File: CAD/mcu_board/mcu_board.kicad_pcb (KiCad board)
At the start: 2 copper layers, 151 parts, among them J1 2.1MM BARREL, J2 E5908-5VC145-L, J3 E5908-5VC145-L, J4 E5908-5VC145-L, SW1 SW_EN, U1 Teensy3.6, U2 AUDIOSHIELD, U3 LM1117-ADJ, U4 TLC5947DAP

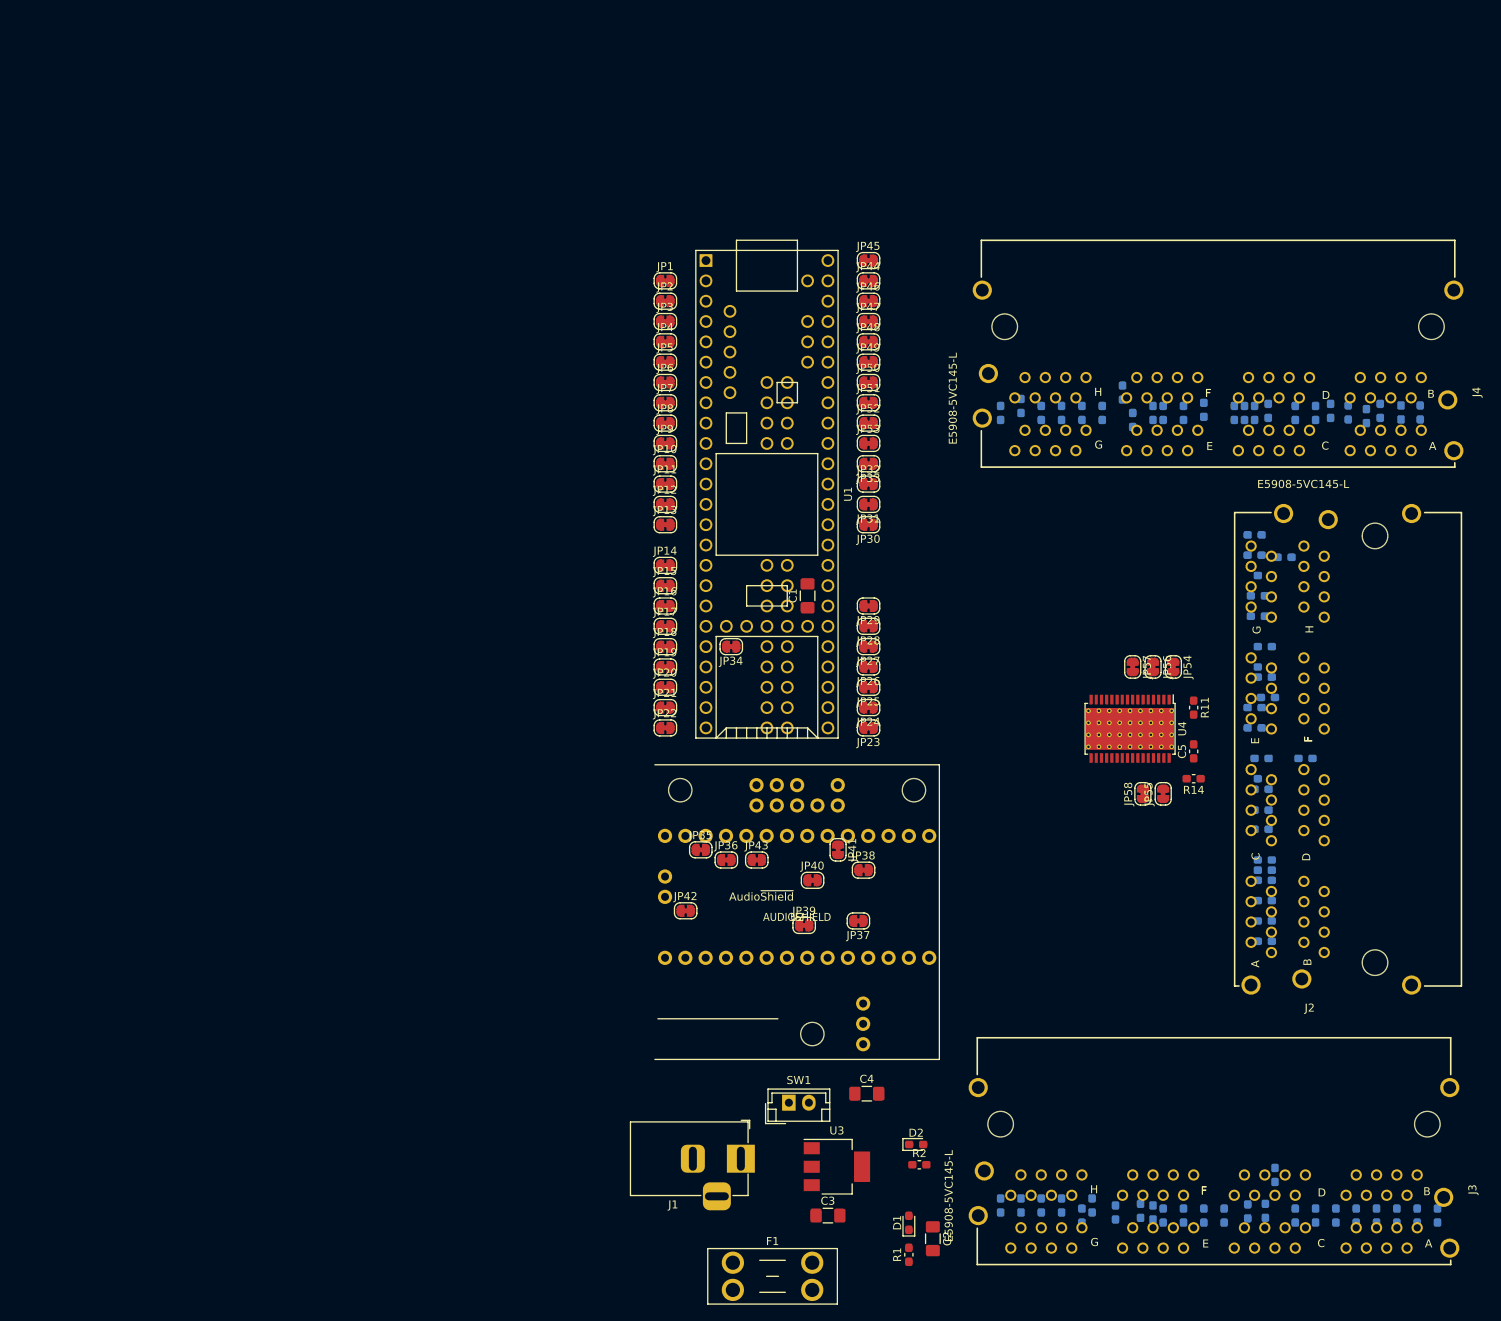
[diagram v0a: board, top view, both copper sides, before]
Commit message: finishes most routing
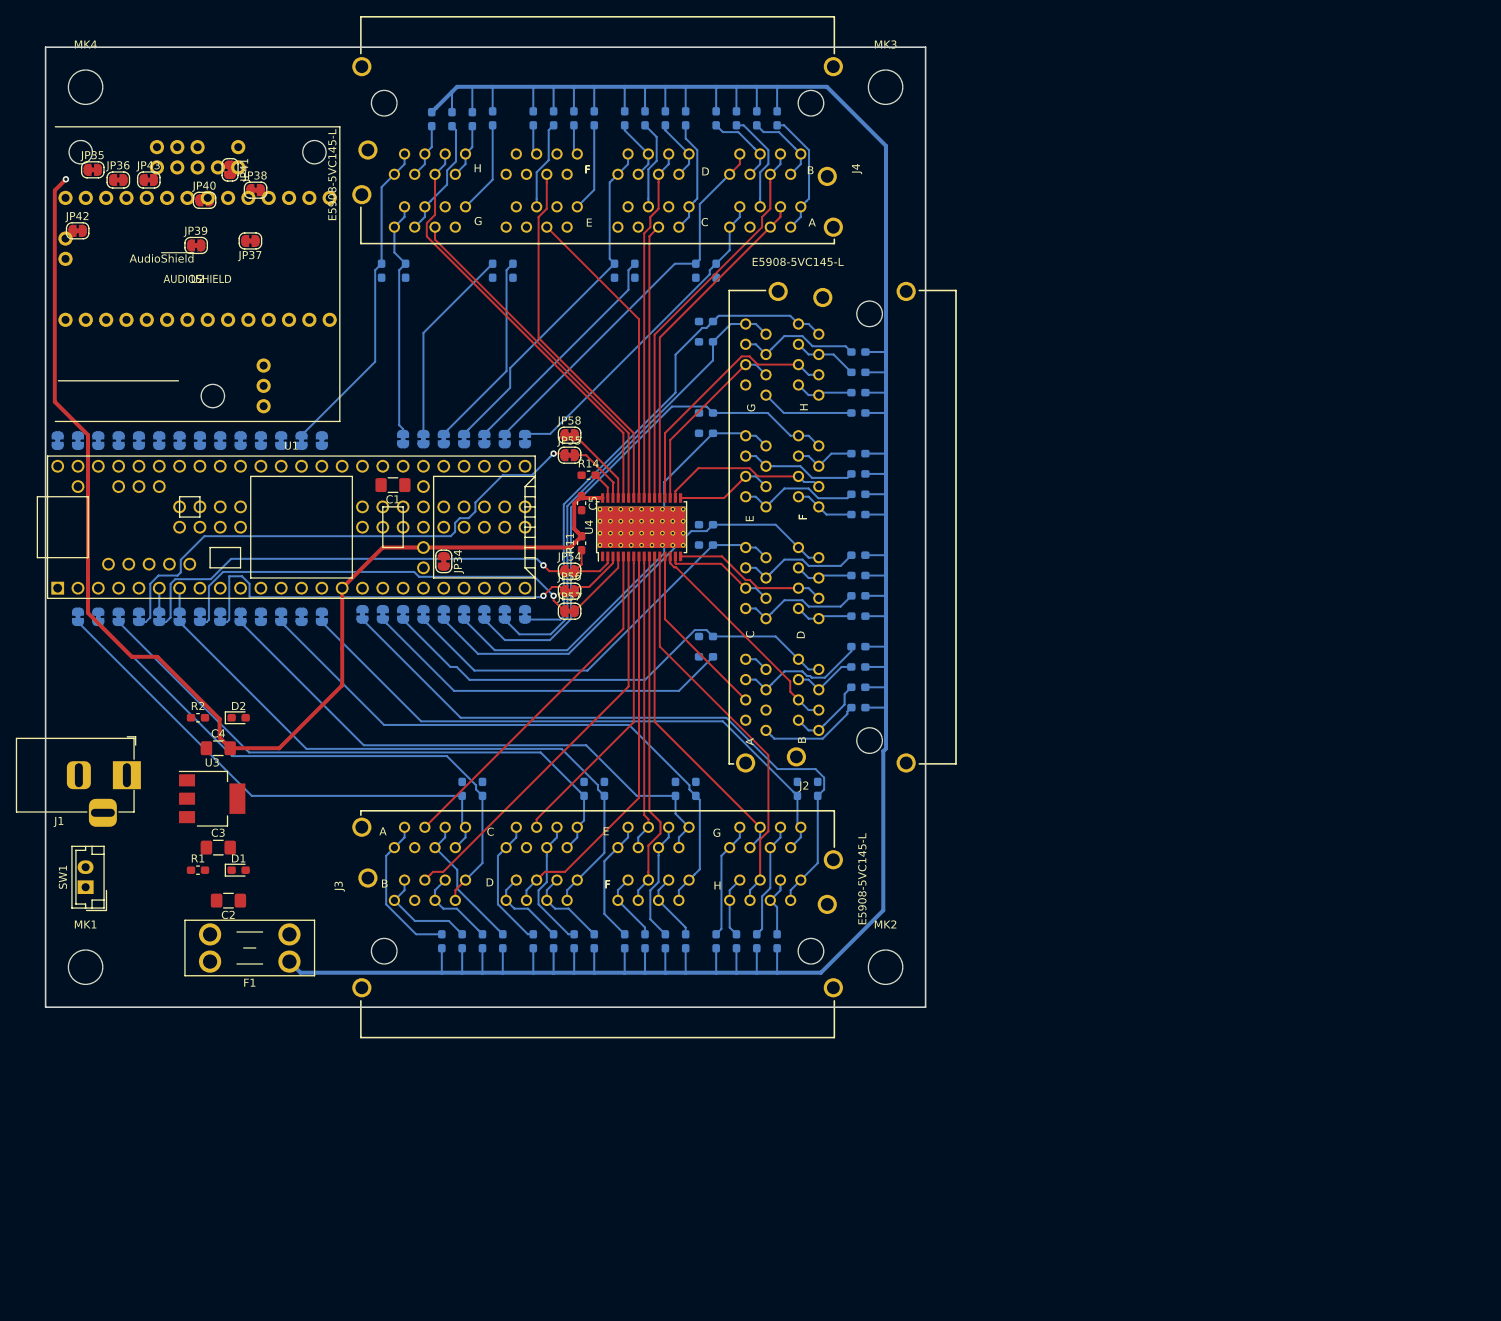
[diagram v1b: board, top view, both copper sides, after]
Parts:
- added MK1: Mounting_Hole, MountingHole:MountingHole_4.3mm_M4, F.Cu at (5.00, 115.0)
- added MK2: Mounting_Hole, MountingHole:MountingHole_4.3mm_M4, F.Cu at (105.0, 115.0)
- added MK3: Mounting_Hole, MountingHole:MountingHole_4.3mm_M4, F.Cu at (105.0, 5.00)
- added MK4: Mounting_Hole, MountingHole:MountingHole_4.3mm_M4, F.Cu at (5.00, 5.00)
- JP1, JP10, JP11, JP12, JP13, JP14, JP15, JP16, JP17, JP18, JP19, JP2, JP20, JP21, JP22, JP23, JP24, JP25, JP26, JP27, JP28, JP29, JP3, JP30, JP31, JP32, JP33, JP4, JP44, JP45, JP46, JP47, JP48, JP49, JP5, JP50, JP51, JP52, JP53, JP6, JP7, JP8, JP9: moved to B.Cu
- moved R76 126.7 mm to (52.1, 111.8), turned to 270 degrees
- moved R64 126.7 mm to (49.5, 111.8), turned to 270 degrees
- moved R62 123.8 mm to (52.1, 92.7)
- moved R74 119.3 mm to (54.6, 92.7)
- moved R75 116.9 mm to (54.6, 111.8), turned to 90 degrees
- moved R63 116.9 mm to (57.1, 111.8), turned to 90 degrees
- moved JP35 114.0 mm to (5.90, 15.3)
- moved JP36 114.0 mm to (9.09, 16.6)
- moved JP37 114.0 mm to (25.6, 24.2)
- moved JP38 114.0 mm to (26.2, 17.9)
- moved JP39 114.0 mm to (18.8, 24.8)
- moved JP40 114.0 mm to (19.9, 19.1)
- moved JP41 114.0 mm to (23.1, 15.3)
- moved JP42 114.0 mm to (4.01, 22.9)
- moved JP43 114.0 mm to (12.9, 16.6)
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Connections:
- JP1 pad 1: /SW_0 -> /SW_16
- JP11 pad 1: /SW_5 -> /SW_21
- JP13 pad 1: /SW_6 -> /SW_22
- JP14 pad 1: /SW_7 -> /SW_23
- JP2 pad 1: /SW_1 -> /SW_17
- JP23 pad 1: /SW_17 -> /SW_0
- JP24 pad 1: /SW_18 -> /SW_1
- JP25 pad 1: /SW_19 -> /SW_2
- JP26 pad 1: /SW_20 -> /SW_3
- JP27 pad 1: /SW_21 -> /SW_4
- JP28 pad 1: /SW_21 -> /SW_5
- JP29 pad 1: /SW_22 -> /SW_6
- JP3 pad 1: /SW_2 -> /SW_18
- JP31 pad 1: /SW_23 -> /SW_7
- JP6 pad 1: /SW_3 -> /SW_19
- JP9 pad 1: /SW_4 -> /SW_20
- U4 pad 10: /LED_5 -> /LED_21
- U4 pad 11: /LED_6 -> /LED_22
- U4 pad 12: /LED_7 -> /LED_23
- U4 pad 21: /LED_16 -> /LED_0
- U4 pad 22: /LED_17 -> /LED_1
- U4 pad 23: /LED_18 -> /LED_2
- U4 pad 24: /LED_19 -> /LED_3
- U4 pad 25: /LED_20 -> /LED_4
- U4 pad 26: /LED_21 -> /LED_5
- U4 pad 27: /LED_22 -> /LED_6
- U4 pad 28: /LED_23 -> /LED_7
- U4 pad 5: /LED_0 -> /LED_16
- U4 pad 6: /LED_1 -> /LED_17
- U4 pad 7: /LED_2 -> /LED_18
- U4 pad 8: /LED_3 -> /LED_19
- U4 pad 9: /LED_4 -> /LED_20
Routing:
- net +12V: track 0.00 -> 370.5 mm
- net +3V3: track 0.00 -> 153.1 mm, vias 0 -> 1
- net /SW_23: track 0.00 -> 83.0 mm
- net /SW_19: track 0.00 -> 77.4 mm
- net /SW_22: track 0.00 -> 75.6 mm
- net /SW_21: track 0.00 -> 75.5 mm
- net /SW_18: track 0.00 -> 74.5 mm
- net /SW_17: track 0.00 -> 71.8 mm
- net /SW_20: track 0.00 -> 71.1 mm
- net /XLAT: track 0.00 -> 66.7 mm, vias 0 -> 1
- net /SW_13: track 0.00 -> 65.2 mm
- net /SW_15: track 0.00 -> 64.4 mm
- net /SW_16: track 0.00 -> 64.2 mm
- net /SW_9: track 0.00 -> 59.7 mm
- net /SW_14: track 0.00 -> 59.5 mm
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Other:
- board outline added: 110 x 120 mm

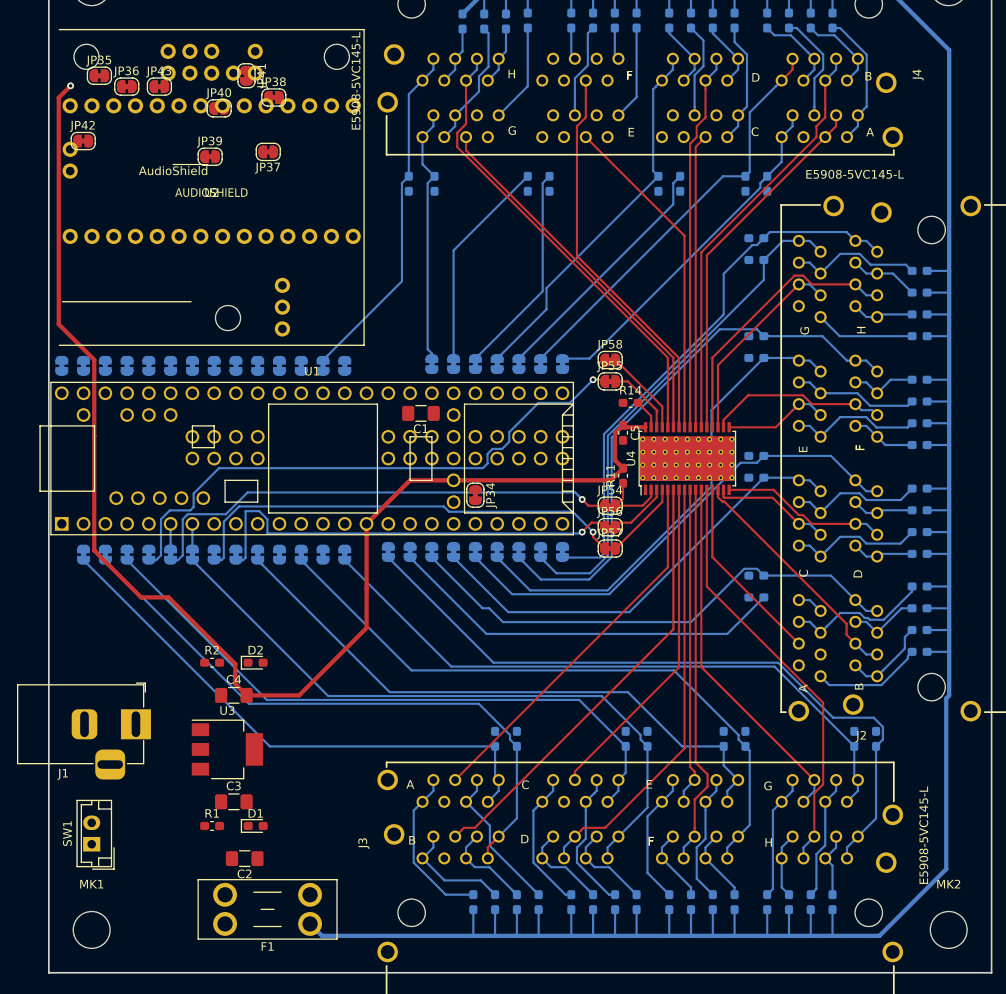
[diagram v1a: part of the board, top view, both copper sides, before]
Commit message: finish all routing but GND
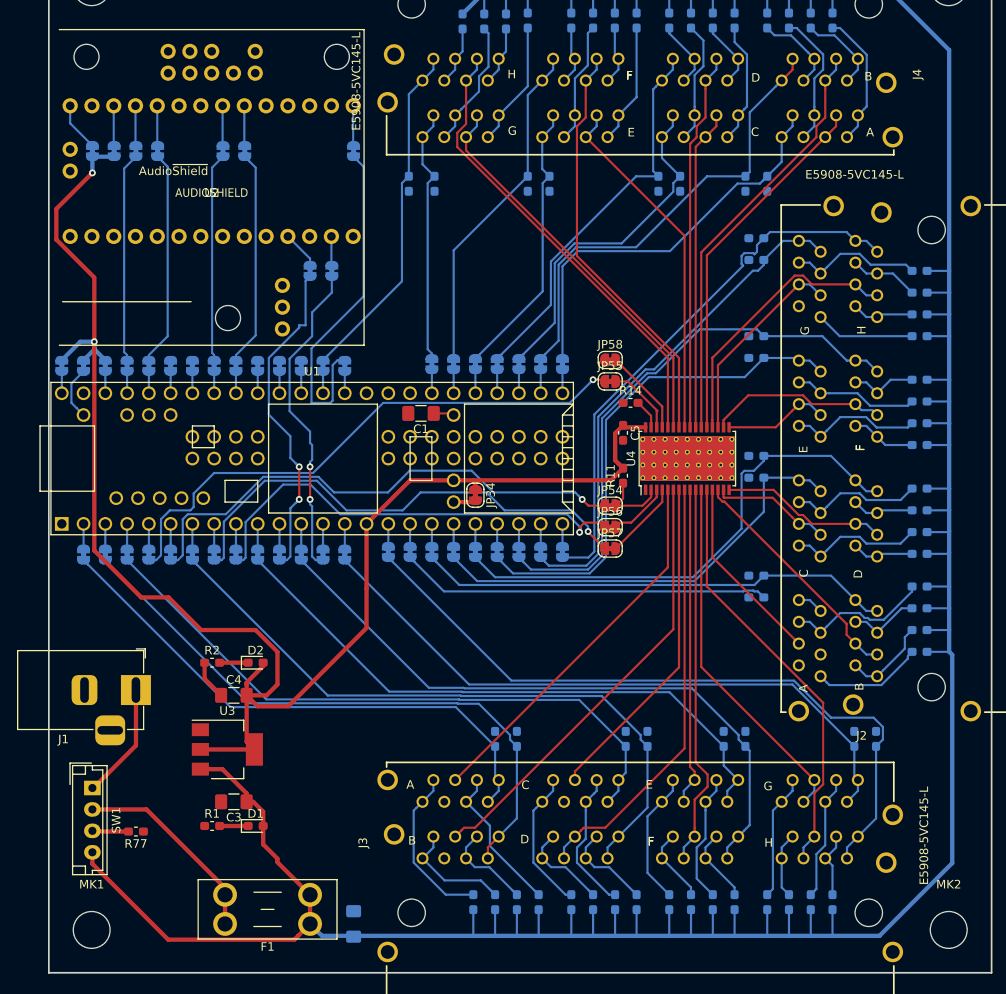
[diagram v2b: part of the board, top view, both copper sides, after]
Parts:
- added R77: 1K, Resistor_SMD:R_0603_1608Metric_Pad1.05x0.95mm_HandSolder, F.Cu at (10.2, 103.5)
- C2, JP35, JP36, JP37, JP38, JP39, JP40, JP41, JP42, JP43: moved to B.Cu
- R70: value R_L -> 1K
- SW1: value SW_EN -> SW_SPST_LED; footprint Connector_JST:JST_EH_B02B-EH-A_1x02_P2.50mm_Vertical -> Connector_JST:JST_EH_B04B-EH-A_1x04_P2.50mm_Vertical
- moved JP38 21.3 mm to (33.0, 38.1), turned to 90 degrees
- moved JP39 16.8 mm to (35.6, 24.1), turned to 90 degrees
- moved C2 14.8 mm to (35.6, 114.3), turned to 90 degrees
- moved JP37 14.7 mm to (30.5, 38.1), turned to 90 degrees
- moved JP41 9.22 mm to (20.3, 24.1), turned to 90 degrees
- moved JP35 8.84 mm to (5.08, 24.1), turned to 90 degrees
- moved JP42 8.77 mm to (12.7, 24.1), turned to 270 degrees
- moved JP43 8.01 mm to (10.2, 24.1), turned to 270 degrees
- moved JP36 7.67 mm to (7.62, 24.1), turned to 90 degrees
- moved SW1 6.56 mm to (5.08, 98.4), turned to 270 degrees
- moved JP40 5.82 mm to (22.9, 24.1), turned to 90 degrees
- moved J1 3.99 mm to (10.2, 87.0)
- turned C3 to 180 degrees
- turned JP32 to 270 degrees
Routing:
- net +12V: track 370.5 -> 427.3 mm
- net /AUDIO_RX: track 0.00 -> 40.1 mm
- net /AUDIO_BCLK: track 0.00 -> 38.5 mm, vias 0 -> 2
- net /AUDIO_MCLK: track 0.00 -> 37.5 mm, vias 0 -> 2
- net +3V3: track 153.1 -> 186.4 mm, vias 1 -> 2
- net /AUDIO_SDA: track 0.00 -> 25.2 mm
- net /AUDIO_TX: track 0.00 -> 25.1 mm
- net /AUDIO_LRCLK: track 0.00 -> 24.5 mm
- net /AUDIO_SCL: track 0.00 -> 24.4 mm
- net Net-(F1-Pad2): track 0.00 -> 23.5 mm
- net /SW_5: track 24.9 -> 39.8 mm
- net Net-(J1-Pad1): track 0.00 -> 13.6 mm
- net /SW_2: track 29.1 -> 40.8 mm
- net /SW_4: track 24.9 -> 32.8 mm
- net Net-(JP44-Pad1): track 0.00 -> 6.27 mm
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
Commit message: FINAL COMMIT FOR GERBERS 180808
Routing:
- net GND: track 4.61 -> 77.5 mm, vias 0 -> 66
- net +12V: track 427.3 -> 433.2 mm
- net /LED_8: track 22.1 -> 27.2 mm
- net /SW_8: track 46.3 -> 50.6 mm
- net /SW_11: track 59.5 -> 55.9 mm
- net /LED_17: track 51.8 -> 54.8 mm
- net Net-(J2-PadA7): track 12.9 -> 15.9 mm
- net /LED_16: track 44.1 -> 47.2 mm
- net Net-(J2-PadG7): track 11.6 -> 14.7 mm
- net /LED_18: track 38.9 -> 42.0 mm
- net /SW_23: track 83.0 -> 85.3 mm
- net /LED_14: track 23.6 -> 25.0 mm
- net /LED_15: track 32.3 -> 33.1 mm
- net /LED_0: track 42.6 -> 43.3 mm
- net /LED_1: track 49.5 -> 50.1 mm
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- added copper zone on B.Cu, net GND
- added copper zone on F.Cu, net GND
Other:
- board text added: "12V"
- board text added: "GND"
- board text added: "SPHINX - BURNMAN18 -FITZ- 20180808"
- board text added: "SW+"
- board text added: "SW-"
